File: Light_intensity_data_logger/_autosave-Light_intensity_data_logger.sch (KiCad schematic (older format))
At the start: 23 parts, among them J1 Wire_to_Vbat, Q1 NTJD4001NT1G, Q2 NTJD4001NT1G, U1 BME280, U2 TCS34725FN, U3 TSL25911FN, U4 Teensy3.6

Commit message: Teensy flipped sensors rewired
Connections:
- net 17: now also C2.1, U3.5 (Vdd); no longer Q2.5 (G2)
- net 21*: now also U2.5 (INT); no longer U3.2 (INT)
- net 22*: no longer U2.5 (INT)
- net 34: no longer C1.2, U1.2 (CSB), U1.5 (SDO), U1.6 (VDDIO), U1.8 (VDD)
- net 35: no longer C2.1, U3.5 (Vdd)
- net 36: now also Q2.5 (G2); no longer C3.2, U2.1 (VDD)
- net 33*: now reaches U4.30 (33_A14_CAN1TX_SCL0)
- net 33*: now also U3.2 (INT)
- net 20: now reaches U4.47 (20_A6_PWM_CS0_SCK1)
- net 20: now also C1.2, U1.2 (CSB), U1.5 (SDO), U1.6 (VDDIO), U1.8 (VDD)
- net 23: now reaches U4.50 (23_A9_PWM_TOUCH)
- net 23: now also C3.2, U2.1 (VDD)
- no-connect marks 46 -> 43
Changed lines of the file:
@@
 Text Label 10950 4350 0    50   ~ 0
 Vin
-$Comp
-L power:GND #PWR0101
-U 1 1 5E1EC75C
-P 5500 5950
-F 0 "#PWR0101" H 5500 5700 50  0001 C CNN
-F 1 "GND" H 5505 5777 50  0000 C CNN
-F 2 "" H 5500 5950 50  0001 C CNN
-F 3 "" H 5500 5950 50  0001 C CNN
-	1    5500 5950
-	1    0    0    -1
-$EndComp
-$Comp
-L Ben_custom:BU2032SM-BT-GTR BT1
-U 1 1 5E1F3175
-P 5500 5650
-F 0 "BT1" H 5454 5780 50  0000 L CNN
-F 1 "BU2032SM-BT-GTR" H 5250 5850 50  0000 L CNN
-F 2 "Ben_Custom:BU2032SM-BT-GTR" H 5150 5200 50  0001 L BNN
-F 3 "http://www.memoryprotectiondevices.com/datasheets/BU2032SM-BT-GTR-datasheet.pdf" H 4900 5300 50  0001 L BNN
-F 4 "BU2032SM-BT-GCT-ND" H 5100 5100 50  0001 L BNN "Part#"
-	1    5500 5650
-	0    1    1    0
-$EndComp
 Text Label 10950 4550 0    50   ~ 0
 3v3
@@
 Text Label 10950 5050 0    50   ~ 0
 SCL0
-Text Label 3450 2950 0    50   ~ 0
-SCL0
 Text Label 8650 4250 2    50   ~ 0
 SDA1
@@
 	1    2650 1350
 	0    1    1    0
-$EndComp
-$Comp
-L device:D D1
-U 1 1 5E2E8394
-P 5500 4400
-F 0 "D1" V 5600 4500 50  0000 C CNN
-F 1 "D" V 5500 4550 50  0000 C CNN
-F 2 "Diodes_SMD:D_SOD-323" H 5500 4400 50  0001 C CNN
-F 3 "https://toshiba.semicon-storage.com/info/docget.jsp?did=14077&prodName=CUS10S30" H 5500 4400 50  0001 C CNN
-F 4 "CUS10S30H3FCT-ND" H 5500 4400 50  0001 C CNN "Part#"
-	1    5500 4400
-	0    -1   1    0
 $EndComp
 Wire Wire Line
@@
 Current test
 Wire Wire Line
-	5500 4550 5500 4950
-Wire Wire Line
 	5700 5350 5600 5350
 Wire Wire Line
@@
 	5600 4250 5700 4250
 Connection ~ 5500 5350
-Text Label 3200 1900 2    50   ~ 0
-34
 Text Label 8650 4850 2    50   ~ 0
 A0
@@
 Text Label 5300 5250 2    50   ~ 0
 16*
-Text Label 5900 5250 0    50   ~ 0
+Text Label 4100 1900 0    50   ~ 0
 17
 $Comp
@@
 Text Label 2550 1050 2    50   ~ 0
 5
-NoConn ~ 10950 4650
-NoConn ~ 10950 4950
 $Comp
 L conn:Conn_01x01 J1
@@
 Text Label 6000 3750 0    50   ~ 0
 A1
-Text Label 6000 1900 2    50   ~ 0
+Text Label 5900 5250 0    50   ~ 0
 36
-Text Label 4100 1900 2    50   ~ 0
-35
 Text Label 8650 4050 2    50   ~ 0
 36
@@
 Text Label 8650 2150 2    50   ~ 0
 I2C_Pullup
-Text Label 4800 3050 0    50   ~ 0
-21*
-Text Label 5900 2850 0    50   ~ 0
-22*
 Text Label 8650 3150 2    50   ~ 0
 E
@@
 NoConn ~ 10950 950
 NoConn ~ 10950 850
-NoConn ~ 8650 3750
 NoConn ~ 8650 3650
 NoConn ~ 8650 3550
@@
 Text Label 8650 1550 2    50   ~ 0
 6*
-Text Label 4150 3500 0    50   ~ 0
-SDA1
-Text Label 4750 3500 2    50   ~ 0
-SCL1
+Text Label 3450 3150 0    50   ~ 0
+SDA0
+Text Label 5050 3500 2    50   ~ 0
+SCL0
 Text Label 8650 4150 2    50   ~ 0
 SCL1
@@
 Text Label 10950 5150 0    50   ~ 0
 SDA0
-Text Label 5050 3500 2    50   ~ 0
+Text Label 4750 3500 2    50   ~ 0
+SCL1
+Text Label 4150 3500 0    50   ~ 0
+SDA1
+Wire Wire Line
+	5500 4550 5500 4950
+$Comp
+L power:GND #PWR0101
+U 1 1 5E1EC75C
+P 5500 5950
+F 0 "#PWR0101" H 5500 5700 50  0001 C CNN
+F 1 "GND" H 5505 5777 50  0000 C CNN
+F 2 "" H 5500 5950 50  0001 C CNN
+F 3 "" H 5500 5950 50  0001 C CNN
+	1    5500 5950
+	1    0    0    -1
+$EndComp
+$Comp
+L Ben_custom:BU2032SM-BT-GTR BT1
+U 1 1 5E1F3175
+P 5500 5650
+F 0 "BT1" H 5454 5780 50  0000 L CNN
+F 1 "BU2032SM-BT-GTR" H 5250 5850 50  0000 L CNN
+F 2 "Ben_Custom:BU2032SM-BT-GTR" H 5150 5200 50  0001 L BNN
+F 3 "http://www.memoryprotectiondevices.com/datasheets/BU2032SM-BT-GTR-datasheet.pdf" H 4900 5300 50  0001 L BNN
+F 4 "BU2032SM-BT-GCT-ND" H 5100 5100 50  0001 L BNN "Part#"
+	1    5500 5650
+	0    1    1    0
+$EndComp
+$Comp
+L device:D D1
+U 1 1 5E2E8394
+P 5500 4400
+F 0 "D1" V 5600 4500 50  0000 C CNN
+F 1 "D" V 5500 4550 50  0000 C CNN
+F 2 "Diodes_SMD:D_SOD-323" H 5500 4400 50  0001 C CNN
+F 3 "https://toshiba.semicon-storage.com/info/docget.jsp?did=14077&prodName=CUS10S30" H 5500 4400 50  0001 C CNN
+F 4 "CUS10S30H3FCT-ND" H 5500 4400 50  0001 C CNN "Part#"
+	1    5500 4400
+	0    -1   1    0
+$EndComp
+Text Label 3450 2950 0    50   ~ 0
 SCL0
-Text Label 3450 3150 0    50   ~ 0
-SDA0
 Text Label 5100 3500 0    50   ~ 0
 SDA0
+Text Label 10950 4950 0    50   ~ 0
+20
+Text Label 3200 1900 0    50   ~ 0
+20
+Text Label 10950 4650 0    50   ~ 0
+23
+Text Label 6000 1900 0    50   ~ 0
+23
+Text Label 8650 3750 2    50   ~ 0
+33*
+Text Label 5900 2850 0    50   ~ 0
+21*
+Text Label 4800 3050 0    50   ~ 0
+33*
 $EndSCHEMATC

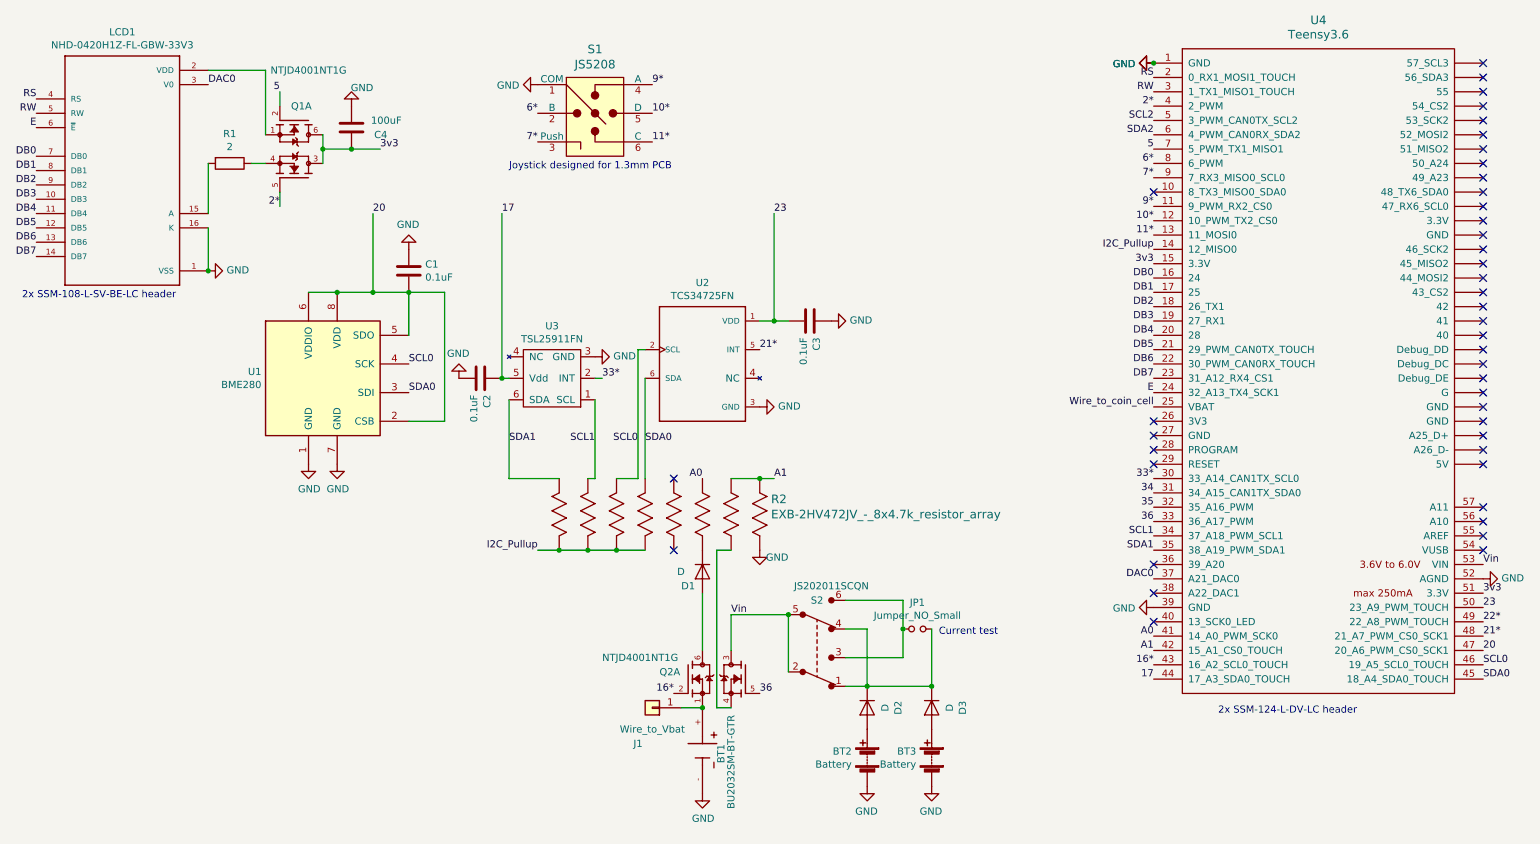
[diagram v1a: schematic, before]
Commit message: All but left monitor wired
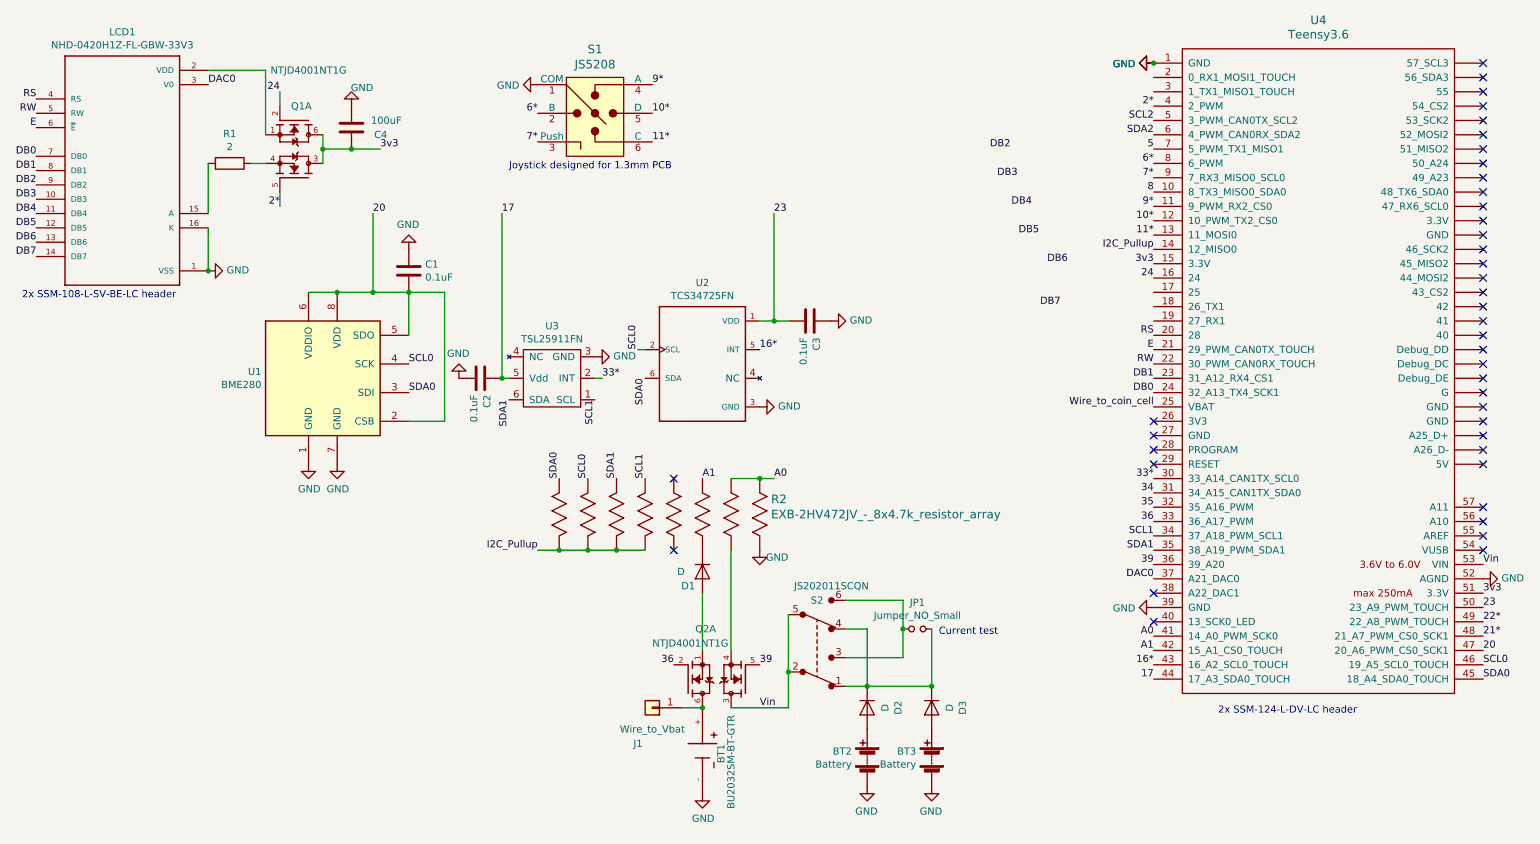
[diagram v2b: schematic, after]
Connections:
- net 16*: now also U2.5 (INT); no longer Q2.2 (G1)
- net 21*: no longer U2.5 (INT)
- net 36: now also Q2.2 (G1); no longer Q2.5 (G2)
- net 5: no longer Q1.2 (G1)
- net A0: now also R2.1, R2.2; no longer R2.3
- net A1: now also R2.3; no longer R2.1, R2.2
- net DB0: now also U4.24 (32_A13_TX4_SCK1); no longer U4.16 (24)
- net DB1: now also U4.23 (31_A12_RX4_CS1); no longer U4.17 (25)
- net DB2: no longer U4.18 (26_TX1)
- net DB3: no longer U4.19 (27_RX1)
- net DB4: no longer U4.20 (28)
- net DB5: no longer U4.21 (29_PWM_CAN0TX_TOUCH)
- net DB6: no longer U4.22 (30_PWM_CAN0RX_TOUCH)
- net DB7: no longer U4.23 (31_A12_RX4_CS1)
- net E: now also U4.21 (29_PWM_CAN0TX_TOUCH); no longer U4.24 (32_A13_TX4_SCK1)
- net RS: now also U4.20 (28); no longer U4.2 (0_RX1_MOSI1_TOUCH)
- net RW: now also U4.22 (30_PWM_CAN0RX_TOUCH); no longer U4.3 (1_TX1_MISO1_TOUCH)
- net SCL0: now also R2.7; no longer R2.6
- net SCL1: now also R2.5; no longer R2.7
- net SDA0: now also R2.8; no longer R2.5
- net SDA1: now also R2.6; no longer R2.8
- net at BT1.+, J1.1 (Pin_1): now also Q2.6 (D1); no longer Q2.1 (S1)
- net at D1.2 (A): now also Q2.1 (S1); no longer Q2.6 (D1)
- net 8: now reaches U4.10 (8_TX3_MISO0_SDA0)
- net 39: now reaches U4.36 (39_A20)
- net 39: now also Q2.5 (G2)
- new net 24: Q1.2 (G1), U4.16 (24)
- no-connect marks 43 -> 41
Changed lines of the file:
@@
 Text Label 8650 4250 2    50   ~ 0
 SDA1
-NoConn ~ 8650 4350
 NoConn ~ 8650 4550
 NoConn ~ 8650 4750
@@
 	5350 5350 5500 5350
 $Comp
-L Ben_custom:NTJD4001NT1G Q2
-U 1 1 5E2C265D
-P 5500 5150
-F 0 "Q2" H 5200 5200 50  0000 L CNN
-F 1 "NTJD4001NT1G" H 4800 5300 50  0000 L CNN
-F 2 "TO_SOT_Packages_SMD:SOT-363_SC-70-6" H 4750 5000 50  0001 L BNN
-F 3 "http://www.onsemi.com/pub/Collateral/NTJD4001N-D.PDF" H 5400 5150 50  0001 L BNN
-F 4 "NTJD4001NT1GOSCT-ND" H 5400 5150 50  0001 L BNN "Part#"
-	1    5500 5150
-	1    0    0    -1
-$EndComp
-$Comp
 L dk_Slide-Switches:JS202011SCQN S2
 U 1 1 5E261D45
@@
 	-1   0    0    -1
 $EndComp
-Text Label 5700 4700 0    50   ~ 0
+Text Label 5900 5350 0    50   ~ 0
 Vin
 $Comp
@@
 Text Notes 7150 4850 0    50   ~ 0
 Current test
-Wire Wire Line
-	5700 5350 5600 5350
-Wire Wire Line
-	5600 5350 5600 4250
-Wire Wire Line
-	5600 4250 5700 4250
-Connection ~ 5500 5350
 Text Label 8650 4850 2    50   ~ 0
 A0
@@
 Text Label 8650 5150 2    50   ~ 0
 17
-Text Label 5300 5250 2    50   ~ 0
+Text Label 5900 2850 0    50   ~ 0
 16*
 Text Label 4100 1900 0    50   ~ 0
@@
 Text Label 2550 1850 2    50   ~ 0
 2*
-Text Label 2550 1050 2    50   ~ 0
-5
 $Comp
 L conn:Conn_01x01 J1
@@
 	-1   0    0    1
 $EndComp
-Wire Wire Line
-	6100 5100 6100 4700
-Connection ~ 6100 4700
-Wire Wire Line
-	5700 4700 5700 4950
 Wire Wire Line
 	4700 4250 4900 4250
@@
 Text Label 8650 1450 2    50   ~ 0
 5
-Text Label 5500 3750 2    50   ~ 0
+Text Label 6000 3750 0    50   ~ 0
 A0
-Text Label 6000 3750 0    50   ~ 0
+Text Label 5500 3750 0    50   ~ 0
 A1
-Text Label 5900 5250 0    50   ~ 0
-36
 Text Label 8650 4050 2    50   ~ 0
 36
@@
 Wire Wire Line
 	6000 3750 5900 3750
-Wire Wire Line
-	5050 3750 4900 3750
 Wire Wire Line
 	5900 2650 6000 2650
@@
 $EndComp
 Connection ~ 8650 850
-Text Label 8650 1050 2    50   ~ 0
+Text Label 8650 2950 2    50   ~ 0
 RW
-Text Label 8650 950  2    50   ~ 0
+Text Label 8650 2750 2    50   ~ 0
 RS
 $Comp
@@
 Text Label 8650 2150 2    50   ~ 0
 I2C_Pullup
+Text Label 8650 2850 2    50   ~ 0
+E
+Text Label 8000 2550 2    50   ~ 0
+DB7
+Text Label 8050 2250 2    50   ~ 0
+DB6
+Text Label 7850 2050 2    50   ~ 0
+DB5
+Text Label 7800 1850 2    50   ~ 0
+DB4
+Text Label 7700 1650 2    50   ~ 0
+DB3
+Text Label 7650 1450 2    50   ~ 0
+DB2
+Text Label 8650 3050 2    50   ~ 0
+DB1
 Text Label 8650 3150 2    50   ~ 0
-E
-Text Label 8650 3050 2    50   ~ 0
-DB7
-Text Label 8650 2950 2    50   ~ 0
-DB6
-Text Label 8650 2850 2    50   ~ 0
-DB5
-Text Label 8650 2750 2    50   ~ 0
-DB4
-Text Label 8650 2650 2    50   ~ 0
-DB3
-Text Label 8650 2550 2    50   ~ 0
-DB2
-Text Label 8650 2450 2    50   ~ 0
-DB1
-Text Label 8650 2350 2    50   ~ 0
 DB0
 Text Label 8650 2050 2    50   ~ 0
@@
 Wire Wire Line
 	4150 3050 4100 3050
-Wire Wire Line
-	4150 3750 4500 3750
-Wire Wire Line
-	4150 3200 4150 3750
-Wire Wire Line
-	4750 3200 4750 3750
-Wire Wire Line
-	4750 3750 4700 3750
 $Comp
 L power:GND #PWR0113
@@
 NoConn ~ 8650 3650
 NoConn ~ 8650 3550
-NoConn ~ 8650 1750
-Wire Wire Line
-	5100 3050 5100 3750
 Text Label 8650 1250 2    50   ~ 0
 SCL2
@@
 Text Label 3450 3150 0    50   ~ 0
 SDA0
-Text Label 5050 3500 2    50   ~ 0
+Text Label 5050 2850 1    50   ~ 0
 SCL0
 Text Label 8650 4150 2    50   ~ 0
@@
 Wire Wire Line
 	4750 3050 4800 3050
-Wire Wire Line
-	5050 2850 5050 3750
 Wire Wire Line
 	5100 2850 5050 2850
@@
 $EndComp
 Connection ~ 7100 5200
-Wire Wire Line
-	5700 4700 6100 4700
 Text Label 10950 5150 0    50   ~ 0
 SDA0
-Text Label 4750 3500 2    50   ~ 0
+Text Label 4750 3200 3    50   ~ 0
 SCL1
-Text Label 4150 3500 0    50   ~ 0
+Text Label 4150 3200 3    50   ~ 0
 SDA1
 Wire Wire Line
@@
 Text Label 3450 2950 0    50   ~ 0
 SCL0
-Text Label 5100 3500 0    50   ~ 0
+Text Label 5100 3050 3    50   ~ 0
 SDA0
 Text Label 10950 4950 0    50   ~ 0
@@
 Text Label 8650 3750 2    50   ~ 0
 33*
-Text Label 5900 2850 0    50   ~ 0
-21*
 Text Label 4800 3050 0    50   ~ 0
 33*
+Text Label 4500 3750 1    50   ~ 0
+SDA0
+Text Label 4700 3750 1    50   ~ 0
+SCL0
+Text Label 4900 3750 1    50   ~ 0
+SDA1
+Text Label 5100 3750 1    50   ~ 0
+SCL1
+Text Label 8650 1750 2    50   ~ 0
+8
+Text Label 5300 5050 2    50   ~ 0
+36
+Text Label 8650 4350 2    50   ~ 0
+39
+Text Label 5900 5050 0    50   ~ 0
+39
+Wire Wire Line
+	6100 5100 6100 5350
+Connection ~ 6100 5100
+Wire Wire Line
+	5700 4950 5700 4250
+$Comp
+L Ben_custom:NTJD4001NT1G Q2
+U 1 1 5E2C265D
+P 5500 5150
+F 0 "Q2" H 5450 4800 50  0000 L CNN
+F 1 "NTJD4001NT1G" H 5150 4900 50  0000 L CNN
+F 2 "TO_SOT_Packages_SMD:SOT-363_SC-70-6" H 4750 5000 50  0001 L BNN
+F 3 "http://www.onsemi.com/pub/Collateral/NTJD4001N-D.PDF" H 5400 5150 50  0001 L BNN
+F 4 "NTJD4001NT1GOSCT-ND" H 5400 5150 50  0001 L BNN "Part#"
+	1    5500 5150
+	1    0    0    1
+$EndComp
+Connection ~ 5500 5350
+Wire Wire Line
+	6100 4700 6100 5100
+Wire Wire Line
+	5700 5350 6100 5350
+Text Label 8650 2350 2    50   ~ 0
+24
+Text Label 2550 1050 2    50   ~ 0
+24
 $EndSCHEMATC
